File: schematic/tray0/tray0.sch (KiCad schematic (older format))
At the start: 16 parts, among them J2 Conn_02x10_Odd_Even, J3 USB_B, P1 Mini-DIN_6pins_ver2, SW1 SW_SPST, U1 ATmega32U4-AU, U2 ST485EBDR, Y1 16MHz

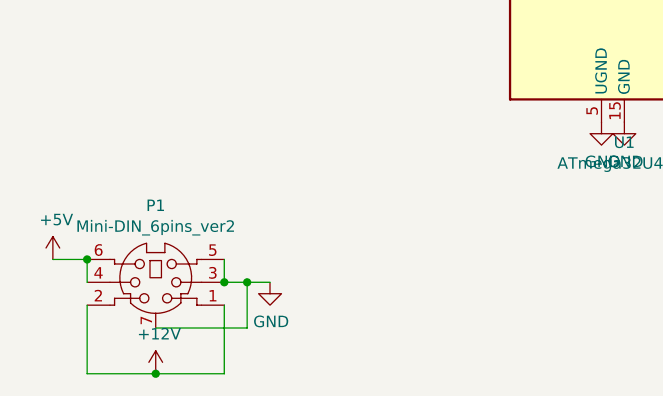
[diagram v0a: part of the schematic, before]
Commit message: Add capacitors to board and change power connector to used by beefier PSU
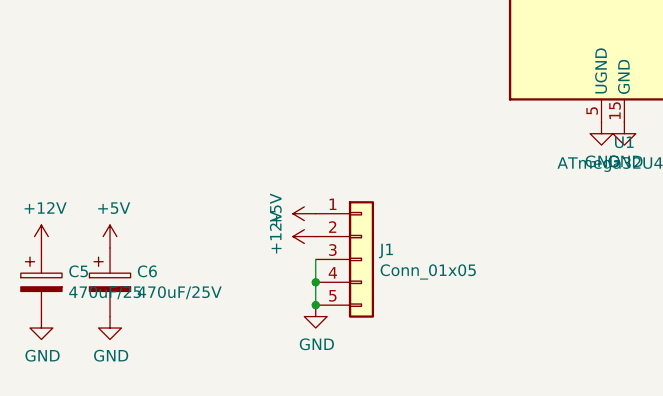
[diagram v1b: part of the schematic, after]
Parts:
- removed P1: Mini-DIN_6pins_ver2, Custom_Footprints:Connector_Mini-DIN_Female_6Pin_2rows, symbol custom_symbols:Mini-DIN_6pins_ver2
- added C5: 470uF/25, Capacitor_THT:CP_Radial_D8.0mm_P3.80mm, symbol Device:CP
- added C6: 470uF/25V, Capacitor_THT:CP_Radial_D8.0mm_P3.80mm, symbol Device:CP
- added J1: Conn_01x05, tray0:PC-MDJ-402-4P, symbol Connector_Generic:Conn_01x05
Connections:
- net +12V: now also C5.1, J1.2 (Pin_2)
- net +5V: now also C6.1, J1.1 (Pin_1)
- net GND: now also C5.2, C6.2, J1.3 (Pin_3), J1.4 (Pin_4), J1.5 (Pin_5)
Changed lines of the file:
@@
 EESchema Schematic File Version 4
-LIBS:tray0-cache
 EELAYER 30 0
 EELAYER END
@@
 L power:+12V #PWR02
 U 1 1 5DEC0860
-P 1700 6450
-F 0 "#PWR02" H 1700 6300 50  0001 C CNN
-F 1 "+12V" H 1715 6623 50  0000 C CNN
-F 2 "" H 1700 6450 50  0001 C CNN
-F 3 "" H 1700 6450 50  0001 C CNN
-	1    1700 6450
-	1    0    0    -1
+P 2400 5850
+F 0 "#PWR02" H 2400 5700 50  0001 C CNN
+F 1 "+12V" H 2415 6023 50  0000 C CNN
+F 2 "" H 2400 5850 50  0001 C CNN
+F 3 "" H 2400 5850 50  0001 C CNN
+	1    2400 5850
+	0    -1   -1   0
 $EndComp
 $Comp
 L power:GND #PWR03
 U 1 1 5DEC1471
-P 2200 6050
-F 0 "#PWR03" H 2200 5800 50  0001 C CNN
-F 1 "GND" H 2205 5877 50  0000 C CNN
-F 2 "" H 2200 6050 50  0001 C CNN
-F 3 "" H 2200 6050 50  0001 C CNN
-	1    2200 6050
+P 2400 6150
+F 0 "#PWR03" H 2400 5900 50  0001 C CNN
+F 1 "GND" H 2405 5977 50  0000 C CNN
+F 2 "" H 2400 6150 50  0001 C CNN
+F 3 "" H 2400 6150 50  0001 C CNN
+	1    2400 6150
 	1    0    0    -1
 $EndComp
@@
 L power:+5V #PWR01
 U 1 1 5DEC1BC5
-P 1250 5950
-F 0 "#PWR01" H 1250 5800 50  0001 C CNN
-F 1 "+5V" H 1265 6123 50  0000 C CNN
-F 2 "" H 1250 5950 50  0001 C CNN
-F 3 "" H 1250 5950 50  0001 C CNN
-	1    1250 5950
-	1    0    0    -1
-$EndComp
-Wire Wire Line
-	1400 5950 1250 5950
-Wire Wire Line
-	1400 6050 1400 5950
-Wire Wire Line
-	1400 6150 1400 6450
-Wire Wire Line
-	1400 6450 1700 6450
-Wire Wire Line
-	1700 6450 2000 6450
-Wire Wire Line
-	2000 6450 2000 6150
-Connection ~ 1700 6450
-Wire Wire Line
-	2000 6050 2100 6050
-Wire Wire Line
-	2000 5950 2000 6050
+P 2400 5750
+F 0 "#PWR01" H 2400 5600 50  0001 C CNN
+F 1 "+5V" H 2415 5923 50  0000 C CNN
+F 2 "" H 2400 5750 50  0001 C CNN
+F 3 "" H 2400 5750 50  0001 C CNN
+	1    2400 5750
+	0    -1   -1   0
+$EndComp
 $Comp
 L MCU_Microchip_ATmega:ATmega32U4-AU U1
@@
 Wire Wire Line
 	2000 1900 2000 2850
-$Comp
-L custom_symbols:Mini-DIN_6pins_ver2 P1
-U 1 1 5DF17C66
-P 1700 6050
-F 0 "P1" H 1700 6385 50  0000 C CNN
-F 1 "Mini-DIN_6pins_ver2" H 1700 6294 50  0000 C CNN
-F 2 "Custom_Footprints:Connector_Mini-DIN_Female_6Pin_2rows" H 1700 6070 50  0001 C CNN
-F 3 "" H 1700 6070 50  0000 C CNN
-	1    1700 6050
-	1    0    0    -1
-$EndComp
-Connection ~ 2000 6050
-Connection ~ 1400 5950
-Wire Wire Line
-	1700 6250 2100 6250
-Wire Wire Line
-	2100 6250 2100 6050
-Connection ~ 2100 6050
-Wire Wire Line
-	2100 6050 2200 6050
 Wire Wire Line
 	4350 3450 4800 3450
@@
 	1    0    0    -1
 $EndComp
+$Comp
+L Connector_Generic:Conn_01x05 J1
+U 1 1 5F954693
+P 2600 5950
+F 0 "J1" H 2680 5992 50  0000 L CNN
+F 1 "Conn_01x05" H 2680 5901 50  0000 L CNN
+F 2 "tray0:PC-MDJ-402-4P" H 2600 5950 50  0001 C CNN
+F 3 "~" H 2600 5950 50  0001 C CNN
+	1    2600 5950
+	1    0    0    -1
+$EndComp
+Wire Wire Line
+	2400 6150 2400 6050
+Connection ~ 2400 6150
+Connection ~ 2400 6050
+Wire Wire Line
+	2400 6050 2400 5950
+$Comp
+L Device:CP C5
+U 1 1 5F963E4E
+P 1200 6050
+F 0 "C5" H 1318 6096 50  0000 L CNN
+F 1 "470uF/25" H 1318 6005 50  0000 L CNN
+F 2 "Capacitor_THT:CP_Radial_D8.0mm_P3.80mm" H 1238 5900 50  0001 C CNN
+F 3 "~" H 1200 6050 50  0001 C CNN
+	1    1200 6050
+	1    0    0    -1
+$EndComp
+$Comp
+L Device:CP C6
+U 1 1 5F964517
+P 1500 6050
+F 0 "C6" H 1618 6096 50  0000 L CNN
+F 1 "470uF/25V" H 1618 6005 50  0000 L CNN
+F 2 "Capacitor_THT:CP_Radial_D8.0mm_P3.80mm" H 1538 5900 50  0001 C CNN
+F 3 "~" H 1500 6050 50  0001 C CNN
+	1    1500 6050
+	1    0    0    -1
+$EndComp
+$Comp
+L power:GND #PWR023
+U 1 1 5F9648C2
+P 1500 6200
+F 0 "#PWR023" H 1500 5950 50  0001 C CNN
+F 1 "GND" H 1505 6027 50  0000 C CNN
+F 2 "" H 1500 6200 50  0001 C CNN
+F 3 "" H 1500 6200 50  0001 C CNN
+	1    1500 6200
+	1    0    0    -1
+$EndComp
+$Comp
+L power:GND #PWR021
+U 1 1 5F964E40
+P 1200 6200
+F 0 "#PWR021" H 1200 5950 50  0001 C CNN
+F 1 "GND" H 1205 6027 50  0000 C CNN
+F 2 "" H 1200 6200 50  0001 C CNN
+F 3 "" H 1200 6200 50  0001 C CNN
+	1    1200 6200
+	1    0    0    -1
+$EndComp
+$Comp
+L power:+12V #PWR020
+U 1 1 5F965400
+P 1200 5900
+F 0 "#PWR020" H 1200 5750 50  0001 C CNN
+F 1 "+12V" H 1215 6073 50  0000 C CNN
+F 2 "" H 1200 5900 50  0001 C CNN
+F 3 "" H 1200 5900 50  0001 C CNN
+	1    1200 5900
+	1    0    0    -1
+$EndComp
+$Comp
+L power:+5V #PWR022
+U 1 1 5F9657A2
+P 1500 5900
+F 0 "#PWR022" H 1500 5750 50  0001 C CNN
+F 1 "+5V" H 1515 6073 50  0000 C CNN
+F 2 "" H 1500 5900 50  0001 C CNN
+F 3 "" H 1500 5900 50  0001 C CNN
+	1    1500 5900
+	1    0    0    -1
+$EndComp
